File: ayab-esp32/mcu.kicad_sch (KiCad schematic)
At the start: 17 parts, among them Q201 AO3400A, SW201 RESET, SW202 BOOTSEL, U201 ESP32-S3-MINI-1

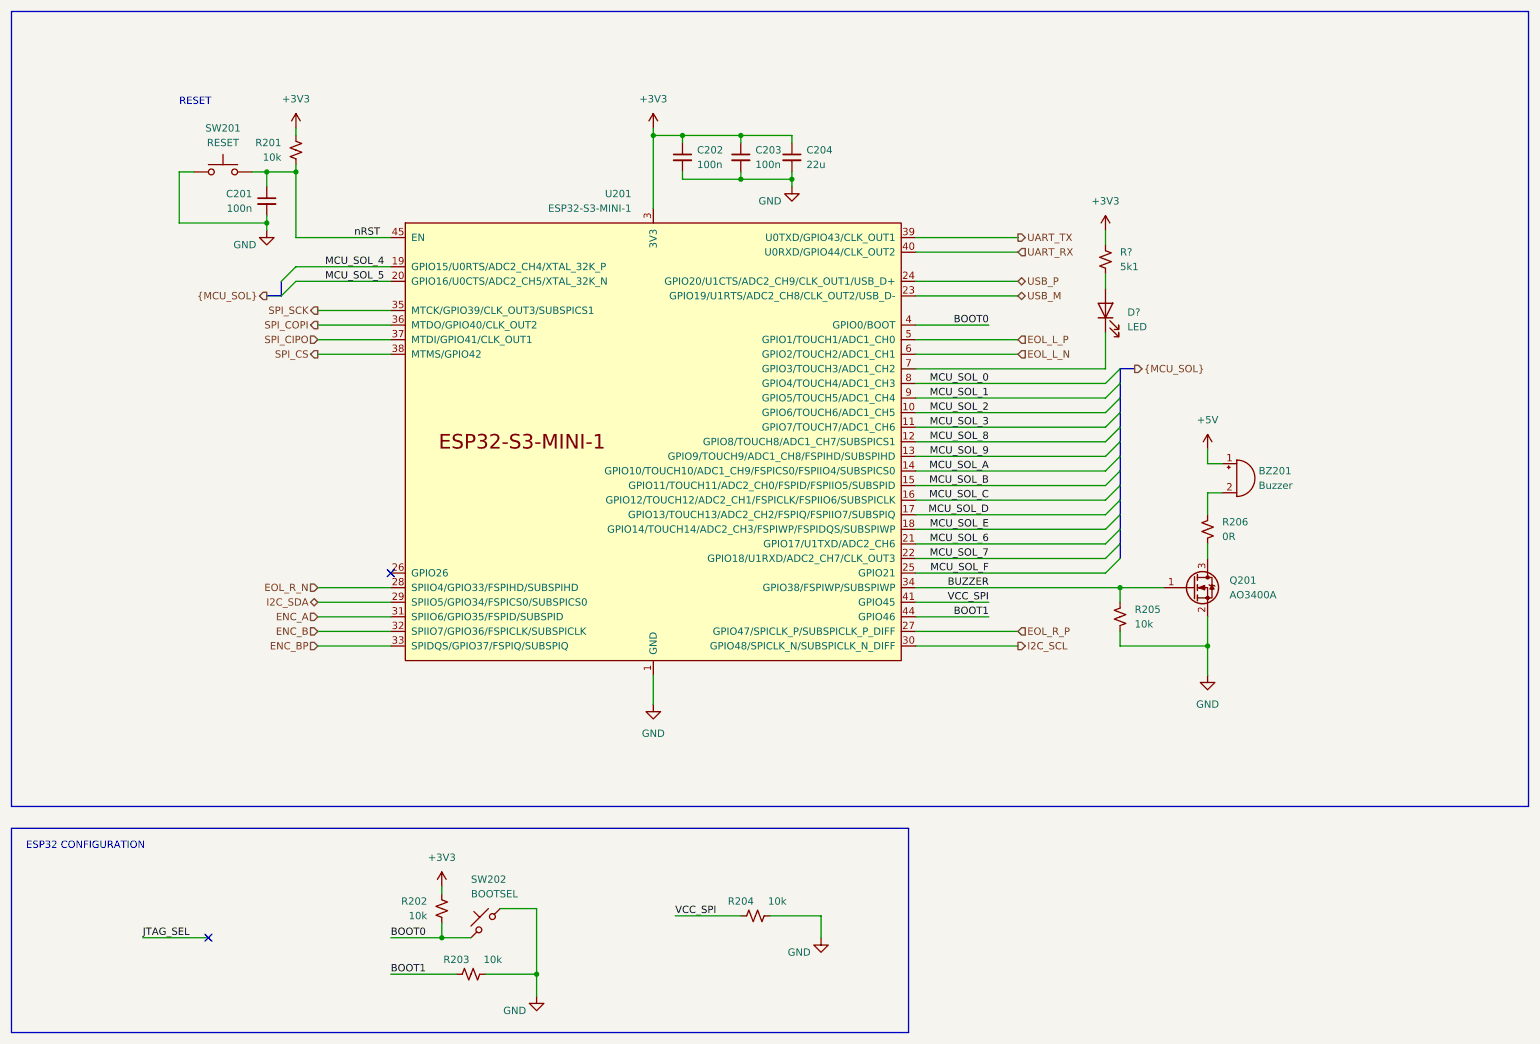
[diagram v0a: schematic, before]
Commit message: fix comparator bias and hysteresis
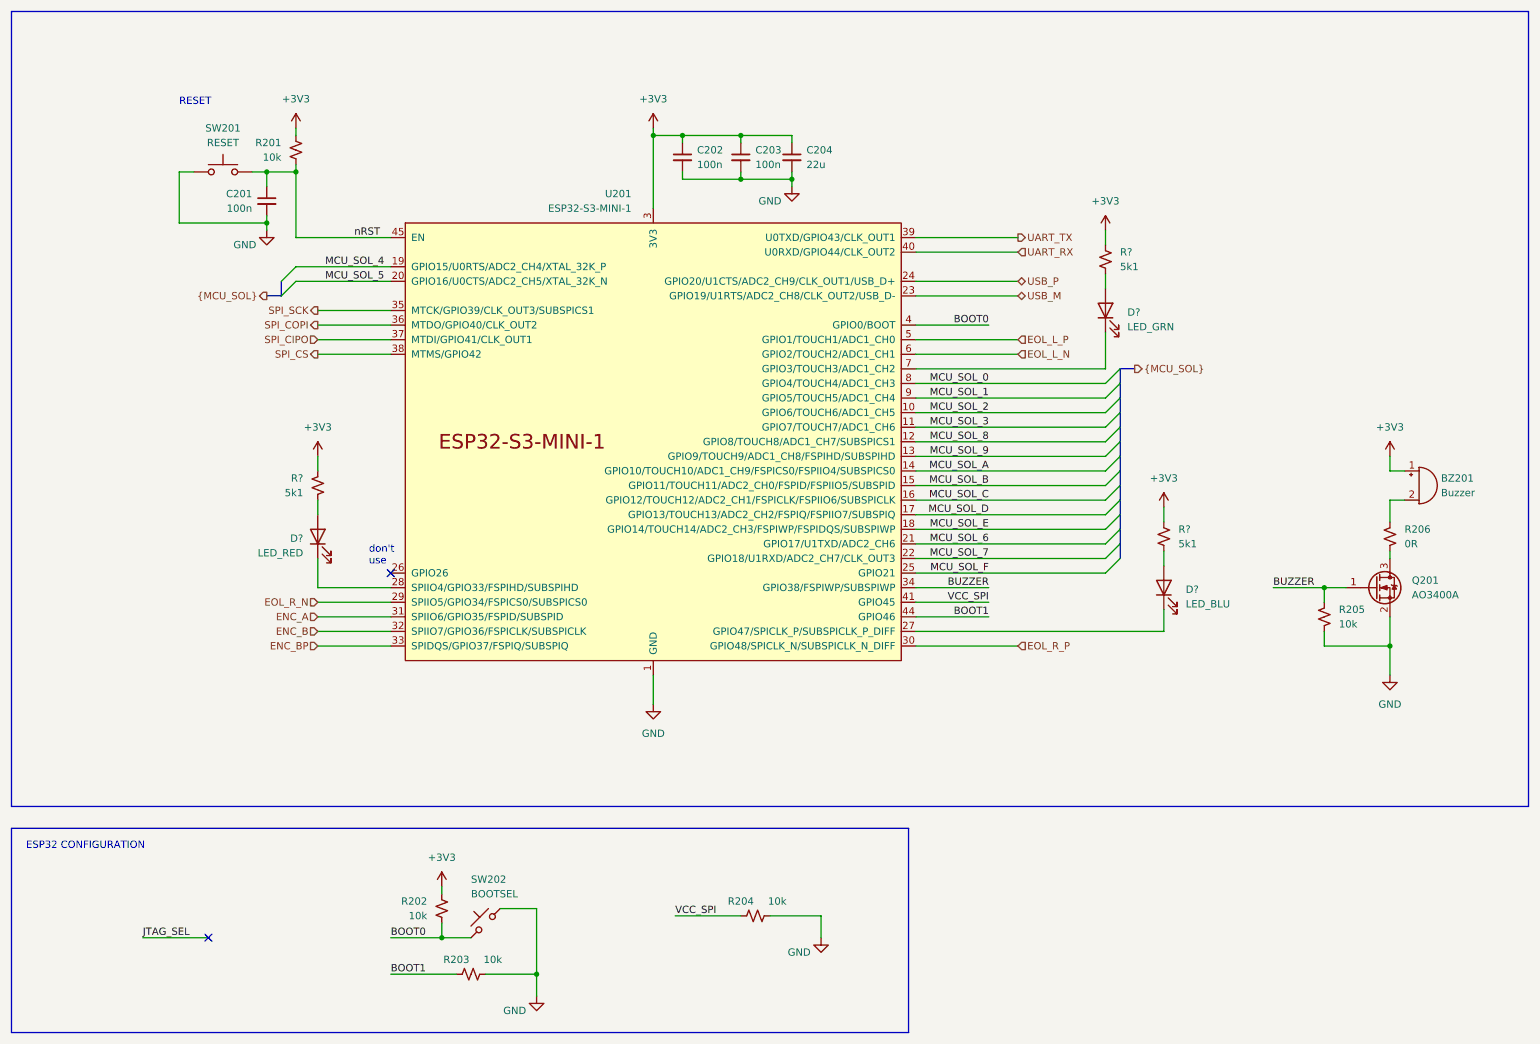
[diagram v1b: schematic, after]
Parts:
- added D?: LED_RED, symbol ayab-esp32:LED
- added D?: LED_BLU, symbol ayab-esp32:LED
- added R? (x2): 5k1, symbol ayab-esp32:R_Small_US
- D?: value LED -> LED_GRN
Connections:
- net +5V is gone; now on net +3V3: BZ201.1 (-)
- net I2C_SCL is gone; now on net EOL_R_P: U201.30 (GPIO48/SPICLK_N/SUBSPICLK_N_DIFF)
- net I2C_SDA is gone; now on net EOL_R_N: U201.29 (SPIIO5/GPIO34/FSPICS0/SUBSPICS0)
- net +3V3: now also R?.1, R?.1
- net EOL_R_N: no longer U201.28 (SPIIO4/GPIO33/FSPIHD/SUBSPIHD)
- net EOL_R_P: no longer U201.27 (GPIO47/SPICLK_P/SUBSPICLK_P_DIFF)
- new net: D?.1 (K), U201.28 (SPIIO4/GPIO33/FSPIHD/SUBSPIHD)
- new net: D?.2 (A), R?.2 (x2)
- new net: D?.1 (K), U201.27 (GPIO47/SPICLK_P/SUBSPICLK_P_DIFF)
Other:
- note added: "don't use"
- moved on the sheet: BZ201, Q201, R205, R206

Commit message: refactor for i2c expander
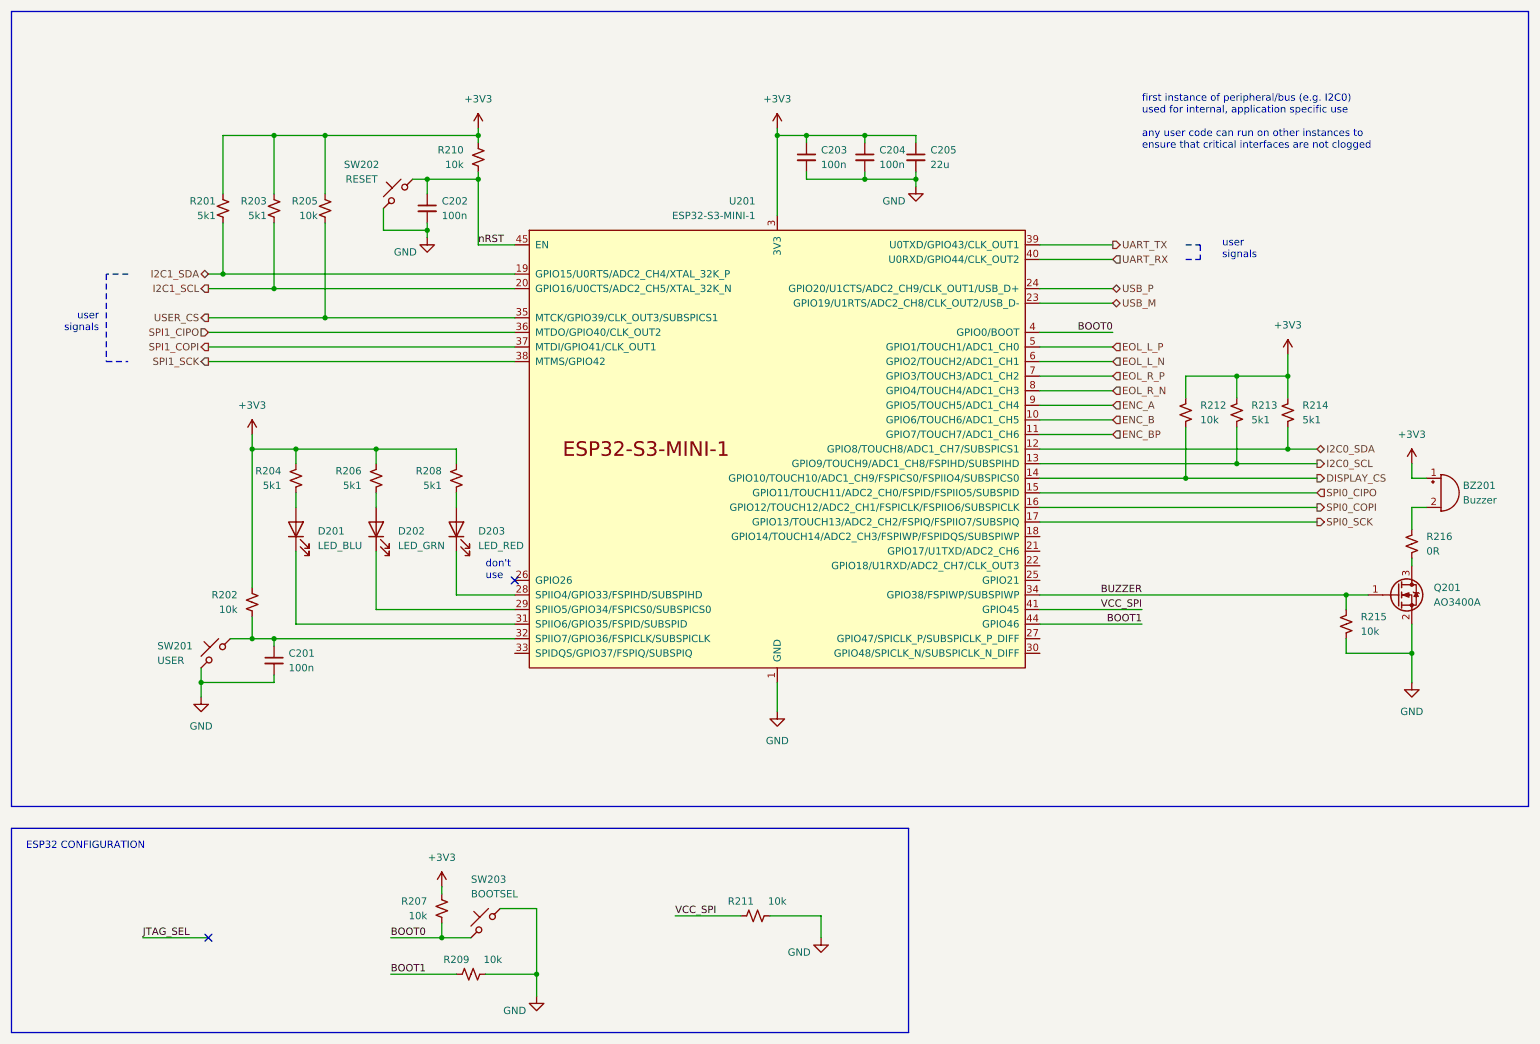
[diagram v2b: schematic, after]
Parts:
- removed D?: LED_RED, symbol ayab-esp32:LED
- added C201: 100n, symbol ayab-esp32:C_Small
- added D203: LED_RED, symbol ayab-esp32:LED
- added R201, R203, R213, R214: 5k1, symbol ayab-esp32:R_Small_US
- added R202, R205, R212: 10k, symbol ayab-esp32:R_Small_US
- added SW201: USER, symbol ayab-esp32:SW_Push_45deg
- SW202: renamed from SW201; symbol ayab-esp32:SW_Push -> ayab-esp32:SW_Push_45deg
- gave numbers to parts that had none: 5
- renumbered C201 to C202, C202 to C203, C203 to C204, C204 to C205, R202 to R207, R203 to R209, R201 to R210, R204 to R211, R205 to R215, R206 to R216, SW202 to SW203
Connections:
- net MCU_SOL_0 is gone; now on net EOL_R_N: U201.8 (GPIO4/TOUCH4/ADC1_CH3)
- net MCU_SOL_1 is gone; now on net ENC_A: U201.9 (GPIO5/TOUCH5/ADC1_CH4)
- net MCU_SOL_2 is gone; now on net ENC_B: U201.10 (GPIO6/TOUCH6/ADC1_CH5)
- net MCU_SOL_3 is gone; now on net ENC_BP: U201.11 (GPIO7/TOUCH7/ADC1_CH6)
- net +3V3: now also R201.1, R202.1, R203.1, R205.1, R212.1, R213.1, R214.1
- net ENC_A: no longer U201.31 (SPIIO6/GPIO35/FSPID/SUBSPID)
- net ENC_B: no longer U201.32 (SPIIO7/GPIO36/FSPICLK/SUBSPICLK)
- net ENC_BP: no longer U201.33 (SPIDQS/GPIO37/FSPIQ/SUBSPIQ)
- net EOL_R_N: no longer U201.29 (SPIIO5/GPIO34/FSPICS0/SUBSPICS0)
- net EOL_R_P: now also U201.7 (GPIO3/TOUCH3/ADC1_CH2); no longer U201.30 (GPIO48/SPICLK_N/SUBSPICLK_N_DIFF)
- net GND: now also C201.2, SW201.1
- net at U201.28 (SPIIO4/GPIO33/FSPIHD/SUBSPIHD): now also D203.1 (K)
- net at R208.2: now also D203.2 (A)
- net at U201.27 (GPIO47/SPICLK_P/SUBSPICLK_P_DIFF): no longer D201.1 (K)
- net at D202.1 (K): now also U201.29 (SPIIO5/GPIO34/FSPICS0/SUBSPICS0); no longer U201.7 (GPIO3/TOUCH3/ADC1_CH2)
- net MCU_SOL_4 renamed I2C1_SDA
- net I2C1_SDA: now also R201.2
- net MCU_SOL_5 renamed I2C1_SCL
- net I2C1_SCL: now also R203.2
- net MCU_SOL_6: no longer names the net of U201.21 (GPIO17/U1TXD/ADC2_CH6)
- net MCU_SOL_7: no longer names the net of U201.22 (GPIO18/U1RXD/ADC2_CH7/CLK_OUT3)
- net MCU_SOL_8 renamed I2C0_SDA
- net I2C0_SDA: now also R214.2
- net MCU_SOL_9 renamed I2C0_SCL
- net I2C0_SCL: now also R213.2
- net MCU_SOL_A renamed DISPLAY_CS
- net DISPLAY_CS: now also R212.2
- net MCU_SOL_B renamed SPI0_CIPO
- net MCU_SOL_C renamed SPI0_COPI
- net MCU_SOL_D renamed SPI0_SCK
- net MCU_SOL_E: no longer names the net of U201.18 (GPIO14/TOUCH14/ADC2_CH3/FSPIWP/FSPIDQS/SUBSPIWP)
- net MCU_SOL_F: no longer names the net of U201.25 (GPIO21)
- net SPI_CIPO renamed SPI1_COPI
- net SPI_COPI renamed SPI1_CIPO
- net SPI_CS renamed SPI1_SCK
- net SPI_SCK renamed USER_CS
- net USER_CS: now also R205.2
- new net: D201.1 (K), U201.31 (SPIIO6/GPIO35/FSPID/SUBSPID)
- new net: C201.1, R202.2, SW201.2, U201.32 (SPIIO7/GPIO36/FSPICLK/SUBSPICLK)
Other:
- note added: "first instance of peripheral/bus (e.g. I2C0) used for internal, application specific use any user code can run on other instances to ensure that critical interfaces are not clogged"
- note added: "user signals"
- note removed: "RESET"
- moved on the sheet: BZ201, C202, C203, C204, C205, D201, D202, Q201, R204, R206, R208, R210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

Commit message: bidirectional level shifting
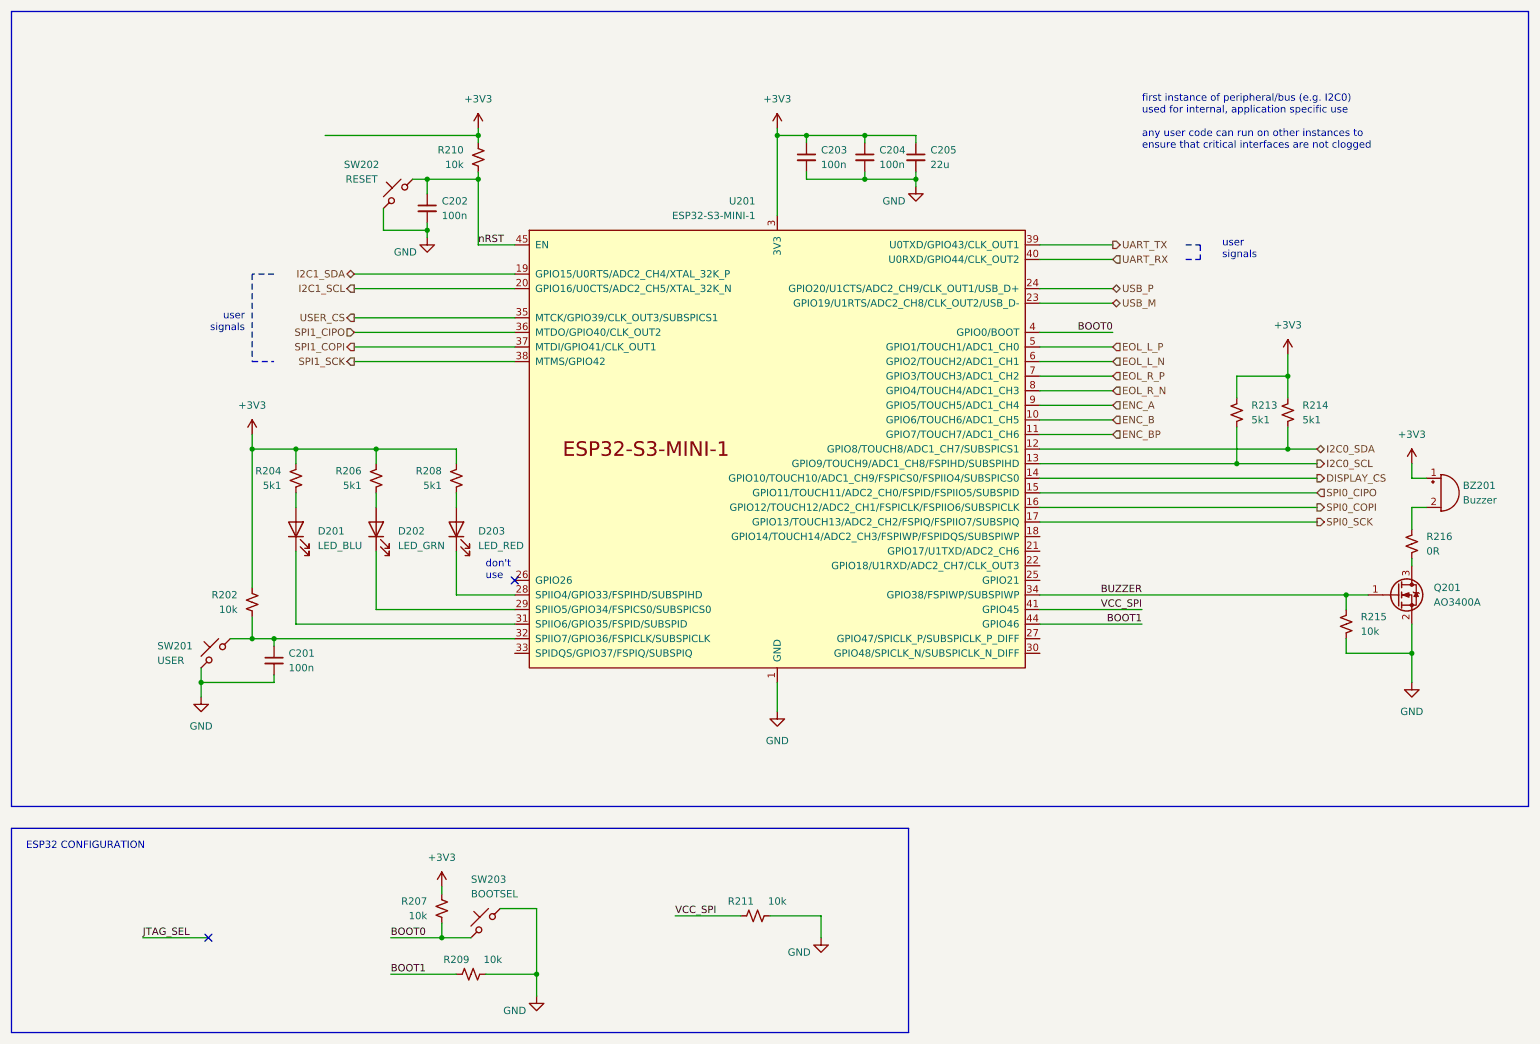
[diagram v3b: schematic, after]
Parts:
- removed R201, R203: 5k1, symbol ayab-esp32:R_Small_US
- removed R205, R212: 10k, symbol ayab-esp32:R_Small_US

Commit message: annotate and terminating resistors
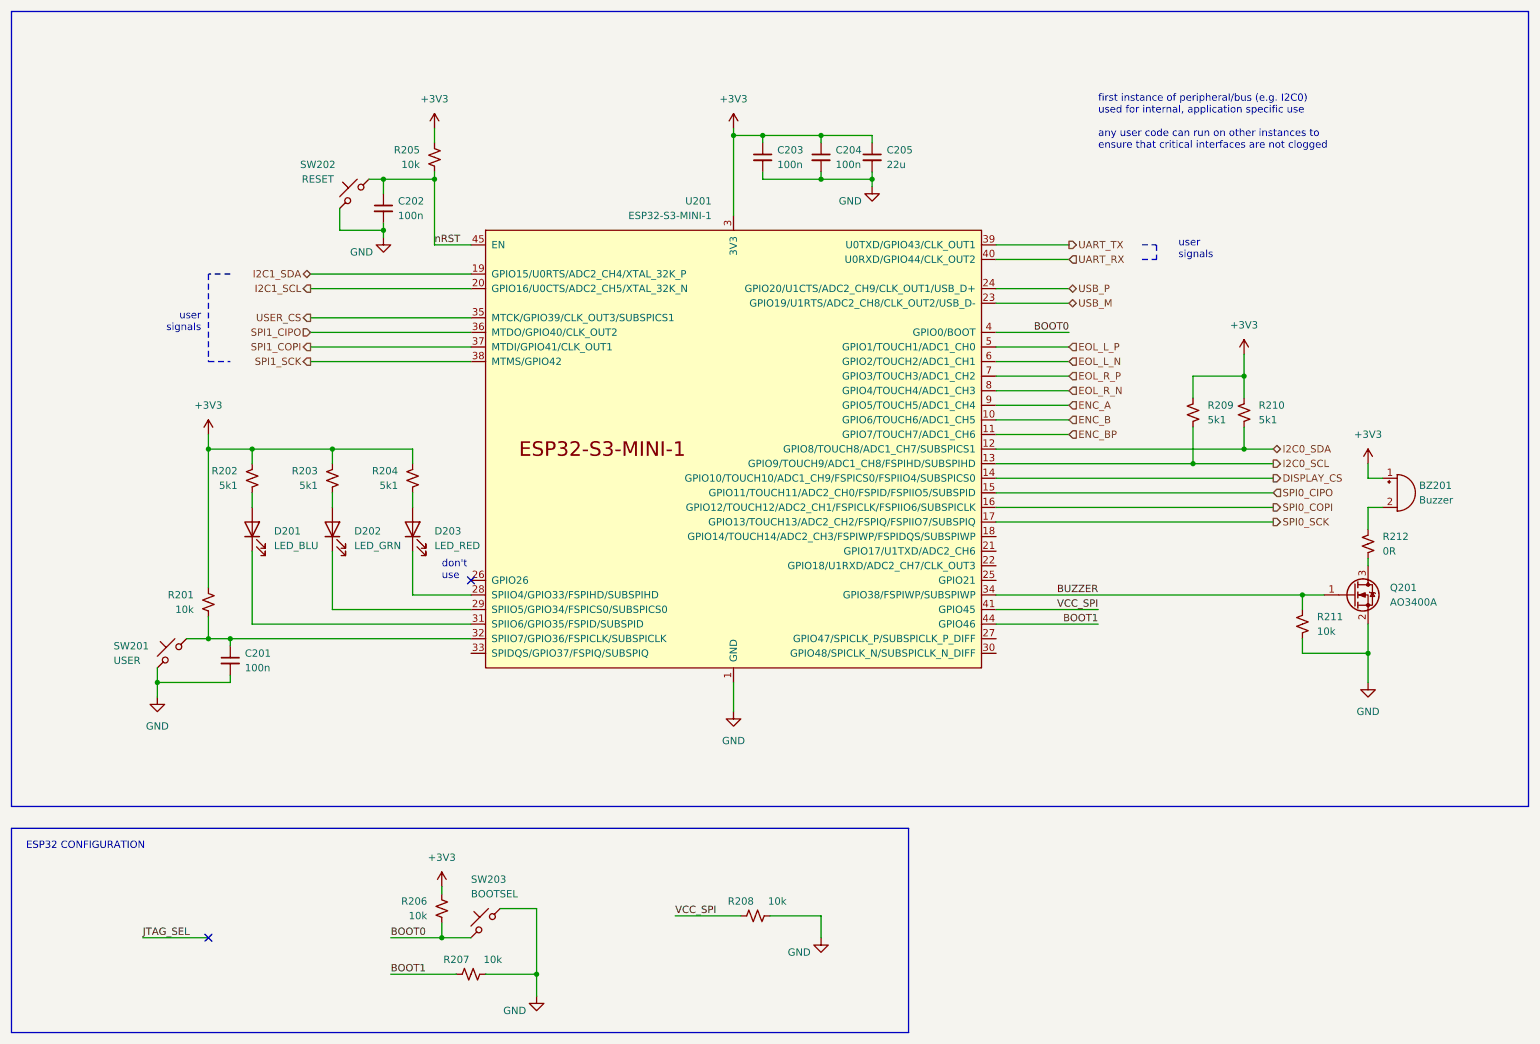
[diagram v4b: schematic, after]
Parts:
- renumbered R202 to R201, R204 to R202, R206 to R203, R208 to R204, R210 to R205, R207 to R206, R209 to R207, R211 to R208, R213 to R209, R214 to R210, R215 to R211, R216 to R212
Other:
- moved on the sheet: BZ201, C201, C202, C203, C204, C205, D201, D202, D203, Q201, R201, R202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
